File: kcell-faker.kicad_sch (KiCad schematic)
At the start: 21 parts, among them J4 DBG, SW1 BOOT, SW2 RST, SW3 UP, SW4 DOWN, SW5 RANGE, U6 ESP32-S3-MINI-1

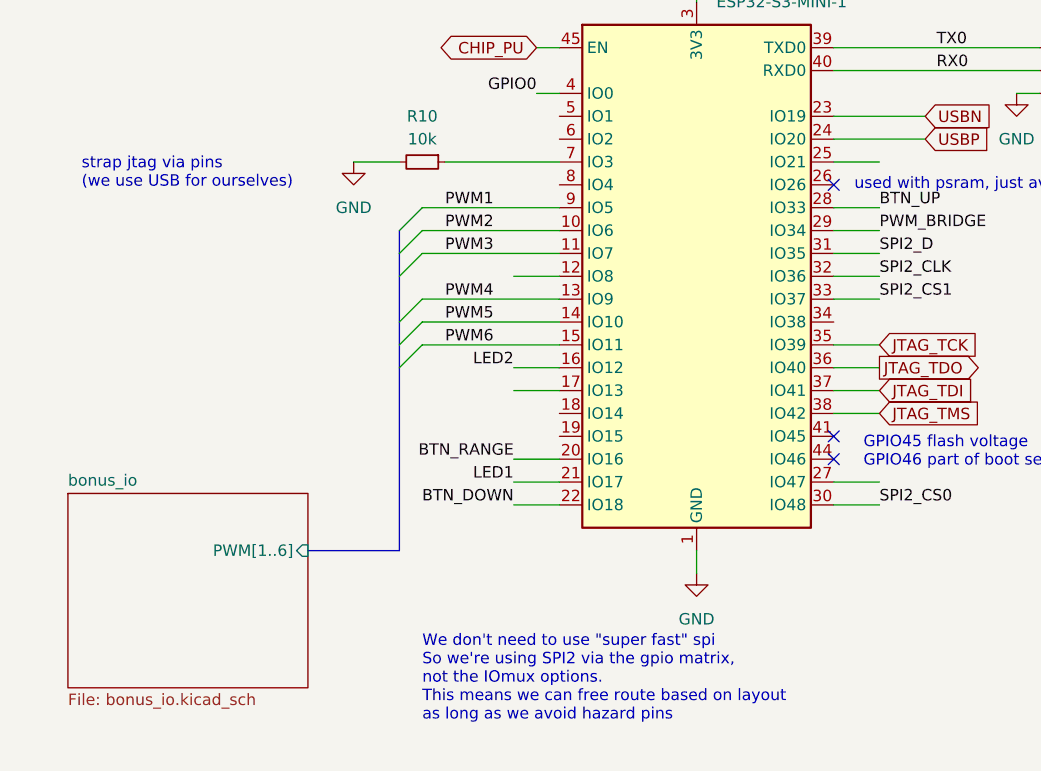
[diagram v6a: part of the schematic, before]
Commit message: add 3 OC outputs
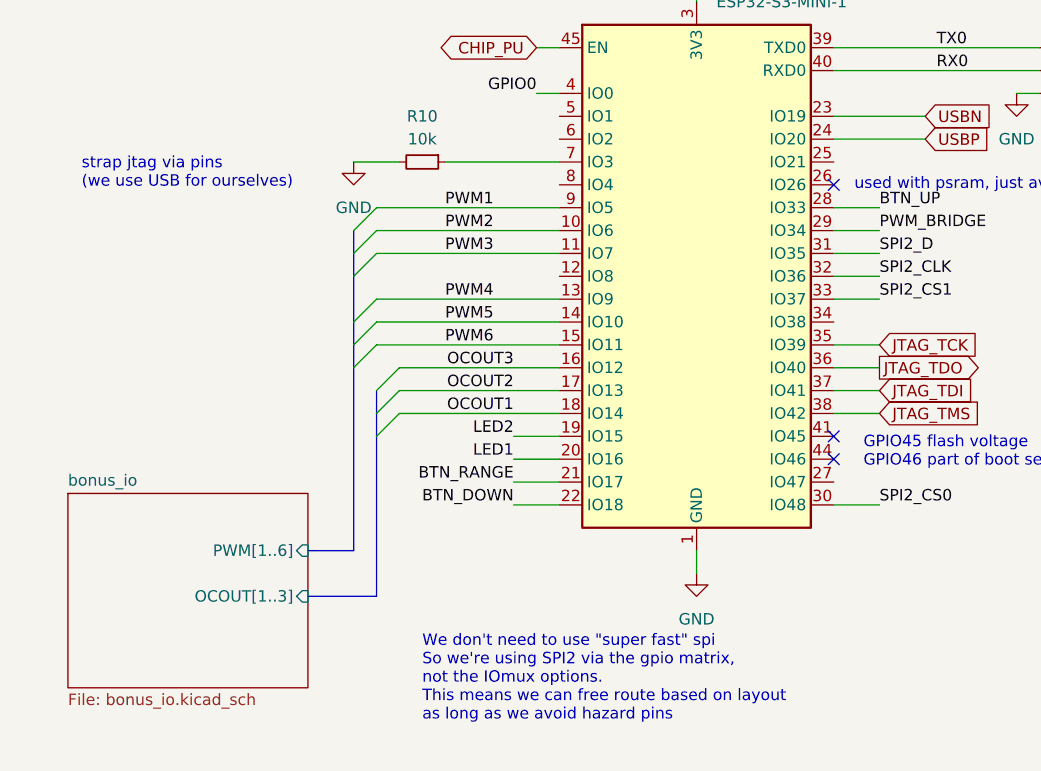
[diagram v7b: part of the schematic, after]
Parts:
- C1: jlcbasic (none) -> basic
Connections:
- net BTN_RANGE: now also U6.21 (IO17); no longer U6.20 (IO16)
- net LED1: now also U6.20 (IO16); no longer U6.21 (IO17)
- net LED2: now also U6.19 (IO15); no longer U6.16 (IO12)
- net OCOUT2: now reaches U6.17 (IO13)
- net OCOUT1: now reaches U6.18 (IO14)
- new net OCOUT3: U6.16 (IO12)
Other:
- sheet bonus_io ports: added OCOUT[1..3]; removed none

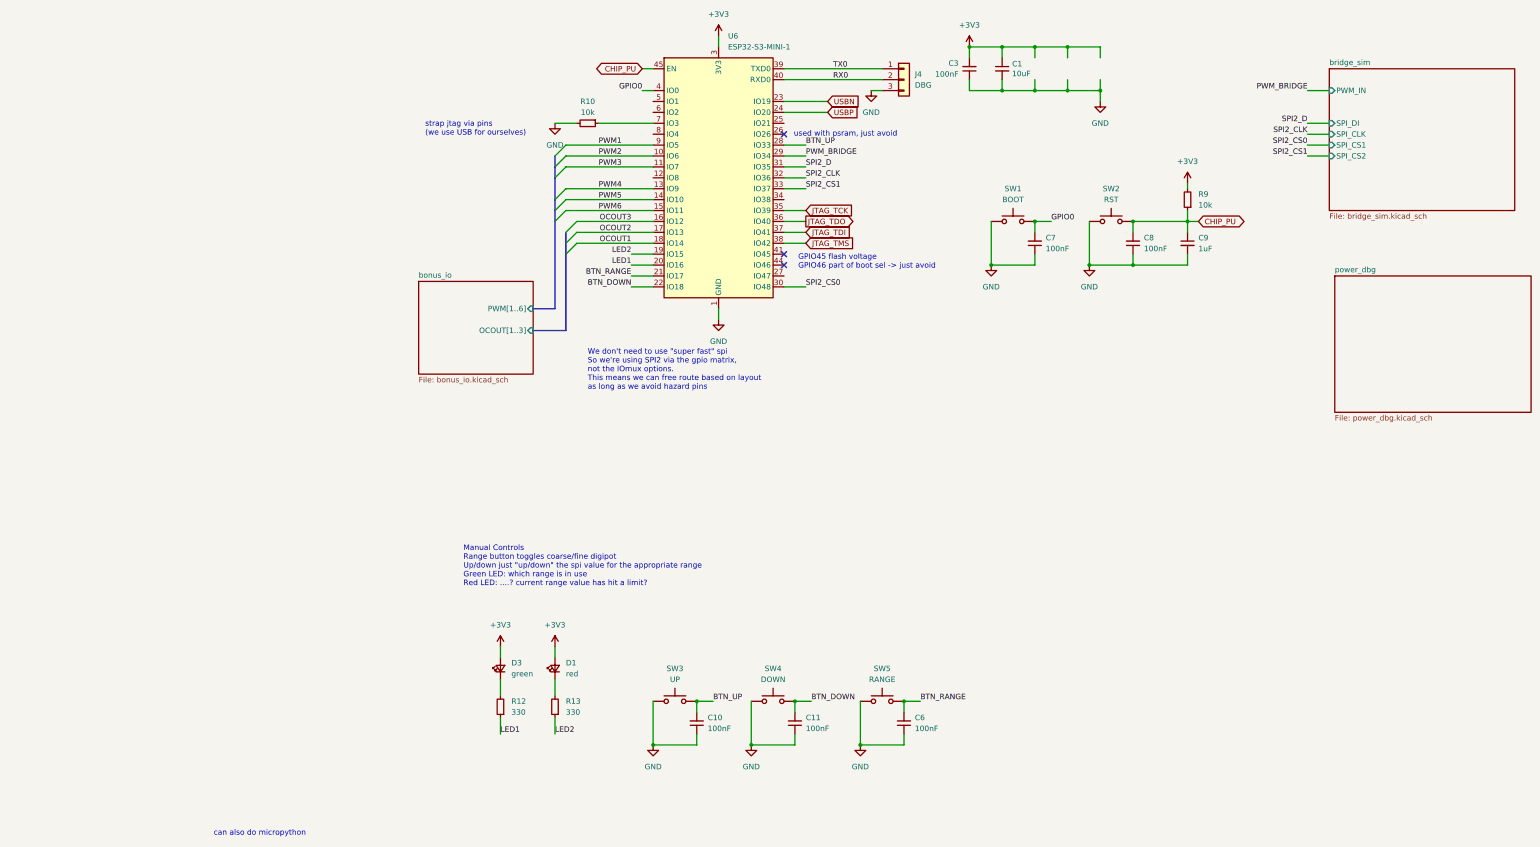
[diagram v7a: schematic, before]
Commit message: overhaul heavily
Move to four connectors for open collector. the uln2303a can then be
used for steppers even if desired.
Relayout the board completely now that we have these extra connectors
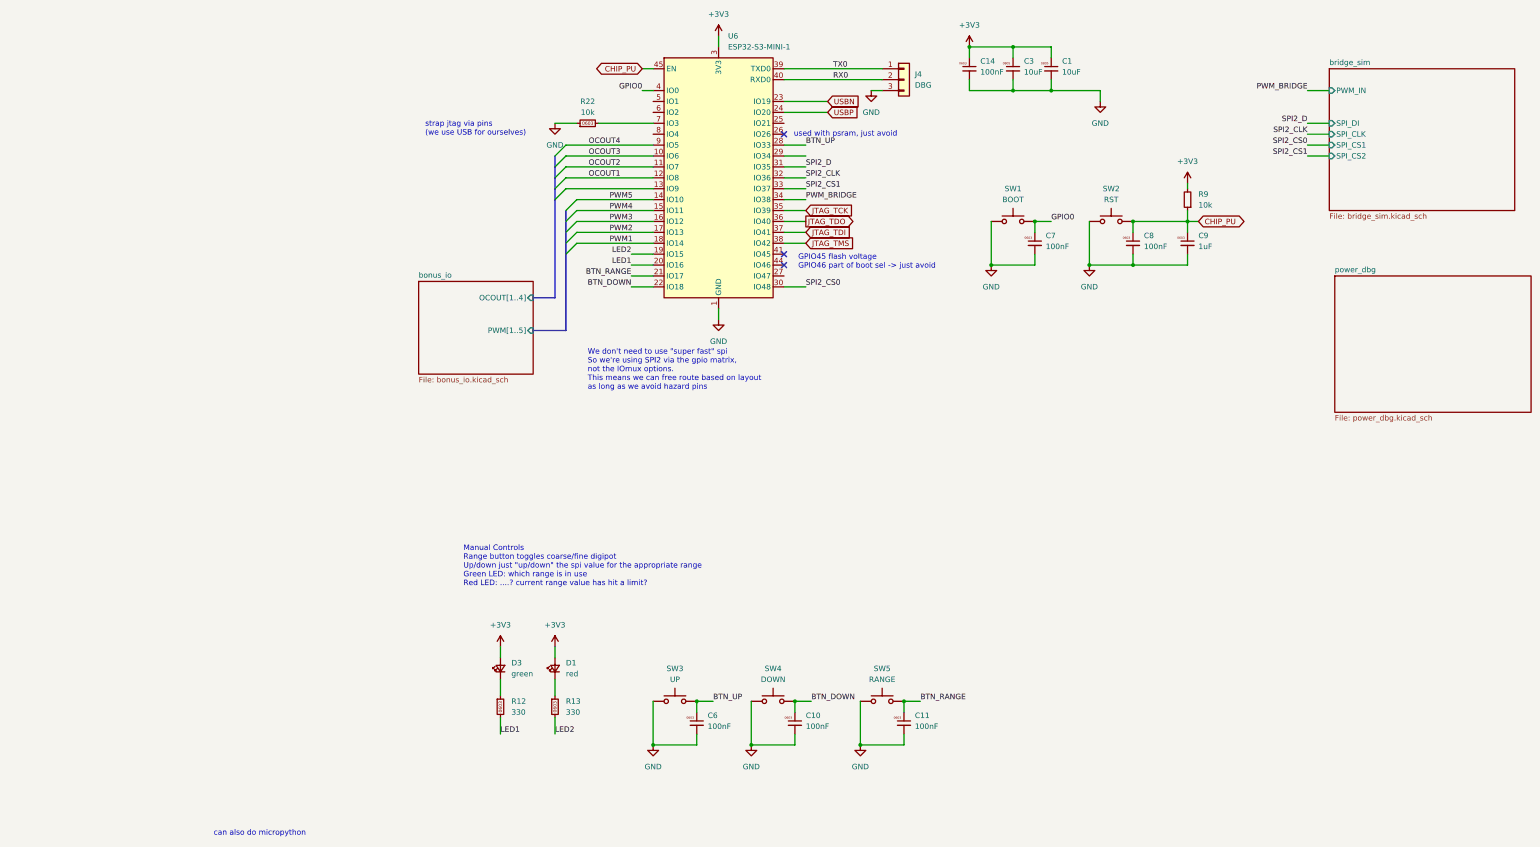
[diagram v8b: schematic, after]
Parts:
- removed C1: 10uF, Capacitor_SMD:C_0805_2012Metric, symbol Device:C_Small
- removed C10, C11, C3, C6, C7, C8: 100nF, Capacitor_SMD:C_0603_1608Metric, symbol Device:C_Small
- removed C9: 1uF, Capacitor_SMD:C_0603_1608Metric, symbol Device:C_Small
- removed R10: 10k, Resistor_SMD:R_0603_1608Metric, symbol Device:R_Small
- removed R12, R13: 330, Resistor_SMD:R_0603_1608Metric, symbol Device:R_Small
- added C1, C3: 10uF, Capacitor_SMD:C_0805_2012Metric, symbol karl-atomic-basic:KC0805_10uF_25V
- added C10, C11, C14, C6, C7, C8: 100nF, Capacitor_SMD:C_0603_1608Metric, symbol karl-atomic-basic:KC0603_100nF
- added C9: 1uF, Capacitor_SMD:C_0603_1608Metric, symbol karl-atomic-basic:KC0603_1uF
- added R12, R13: 330, Resistor_SMD:R_0603_1608Metric, symbol karl-atomic-basic:KR0603_330R
- added R22: 10k, Resistor_SMD:R_0603_1608Metric, symbol karl-atomic-basic:KR0603_10k
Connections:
- net PWM6 is gone; now on net PWM4: U6.15 (IO11)
- net +3V3: now also C1.1, C14.1, C3.1
- net BTN_DOWN: now also C10.1
- net BTN_RANGE: now also C11.1
- net BTN_UP: now also C6.1
- net CHIP_PU: now also C8.1, C9.1
- net GND: now also C1.2, C10.2, C11.2, C14.2, C3.2, C6.2, C7.2, C8.2, C9.2, R22.1
- net GPIO0: now also C7.1
- net LED1: now also R12.2
- net LED2: now also R13.2
- net OCOUT1: now also U6.12 (IO8); no longer U6.18 (IO14)
- net OCOUT2: now also U6.11 (IO7); no longer U6.17 (IO13)
- net OCOUT3: now also U6.10 (IO6); no longer U6.16 (IO12)
- net PWM1: now also U6.18 (IO14); no longer U6.9 (IO5)
- net PWM2: now also U6.17 (IO13); no longer U6.10 (IO6)
- net PWM3: now also U6.16 (IO12); no longer U6.11 (IO7)
- net PWM4: no longer U6.13 (IO9)
- net PWM_BRIDGE: now also U6.34 (IO38); no longer U6.29 (IO34)
- net at U6.7 (IO3): now also R22.2
- net at D3.1 (K): now also R12.1
- net at D1.1 (K): now also R13.1
- new net OCOUT4: U6.9 (IO5)
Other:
- sheet bonus_io ports: added OCOUT[1..4], PWM[1..5]; removed OCOUT[1..3], PWM[1..6]
